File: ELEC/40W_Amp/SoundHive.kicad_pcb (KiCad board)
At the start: 2 copper layers, 5 parts, among them J1 CONN_01X08, J2 CONN_01X08, U1 TPA3106D1

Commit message: Parts and stuff
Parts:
- added C1: 1.0uF, Capacitors_SMD:C_0805, F.Cu at (97.8, 95.2)
- added C2: 1.0uF, Capacitors_SMD:C_0805, F.Cu at (97.8, 100.3)
- L1, L2: value XAL6060-333ME 33uH -> 33uH
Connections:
- U1 pad 19: Net-(U1-Pad19) -> Net-(L1-Pad1)
- U1 pad 20: Net-(U1-Pad20) -> Net-(L1-Pad1)
- U1 pad 21: Net-(U1-Pad21) -> Net-(L2-Pad1)
- U1 pad 22: Net-(U1-Pad22) -> Net-(L2-Pad1)
- U1 pad 3: Net-(U1-Pad3) -> GND
- U1 pad 4: Net-(U1-Pad4) -> GND
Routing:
- net Net-(C1-Pad1): track 0.00 -> 5.85 mm
- net Net-(C2-Pad1): track 0.00 -> 5.74 mm
- added copper zone on F.Cu, net Net-(L2-Pad1)

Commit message: Layout changes, Tall headers added
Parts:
- J1, J2: footprint Pin_Headers:Pin_Header_Straight_1x08_Pitch2.54mm -> Pin_Headers:Pin_Header_Straight_1x08_Tall_Pitch2.54mm

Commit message: Major work.
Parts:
- added C10: 0.22uF, Capacitors_SMD:C_0805, F.Cu at (131.6, 84.3)
- added C11: 0.22uF, Capacitors_SMD:C_0805, F.Cu at (123.4, 111.0)
- added C12: 1nF COG, Capacitors_SMD:C_0805, F.Cu at (102.9, 76.2)
- added C13: 1nF COG, Capacitors_SMD:C_0805, F.Cu at (95.5, 89.2)
- added C14: 1.0uF, Capacitors_SMD:C_0805, F.Cu at (101.6, 72.6)
- added C15: 1.0uF, Capacitors_SMD:C_0805, F.Cu at (116.3, 81.0)
- added C3: 220uF, Capacitors_SMD:CP_Elec_8x10.5, F.Cu at (114.3, 87.9)
- added C4: 1.0uF, Capacitors_SMD:C_0805, F.Cu at (112.3, 106.7)
- added C5: 220uF, Capacitors_SMD:CP_Elec_8x10.5, F.Cu at (114.6, 112.5)
- added C6: 1.0uF, Capacitors_SMD:C_0805, F.Cu at (112.3, 94.2)
- added C7: 1.0uF, Capacitors_SMD:C_0805, F.Cu at (103.9, 108.5)
- added C8: 1.0uF, Capacitors_SMD:C_0805, F.Cu at (105.9, 108.5)
- added C9: 1.0uF, Capacitors_SMD:C_0805, F.Cu at (108.0, 108.5)
- added R1: 100K, Resistors_SMD:R_0805, F.Cu at (98.0, 106.7)
- added R2: 100K, Resistors_SMD:R_0805, F.Cu at (98.0, 108.7)
- added R3: 100K 1%, Resistors_SMD:R_0805, F.Cu at (101.9, 108.5)
- added R4: R, Resistors_SMD:R_0805, F.Cu at (99.8, 84.6)
- added R5: R, Resistors_SMD:R_0805, F.Cu at (91.4, 85.1)
- moved J2 37.0 mm to (123.4, 76.7), turned to 270 degrees
- moved J1 33.7 mm to (101.9, 121.2), turned to 90 degrees
- moved L2 4.57 mm to (120.7, 96.0)
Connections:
- U1 pad 12: Net-(U1-Pad12) -> GND
- U1 pad 14: Net-(U1-Pad14) -> +24V
- U1 pad 15: Net-(U1-Pad15) -> +24V
- U1 pad 16: Net-(U1-Pad16) -> GND
- U1 pad 17: Net-(U1-Pad17) -> GND
- U1 pad 24: Net-(U1-Pad24) -> GND
- U1 pad 25: Net-(U1-Pad25) -> GND
- U1 pad 26: Net-(U1-Pad26) -> +24V
- U1 pad 27: Net-(U1-Pad27) -> +24V
- U1 pad 28: Net-(U1-Pad28) -> +24V
- U1 pad 5: Net-(U1-Pad5) -> /GAIN0
- U1 pad 6: Net-(U1-Pad6) -> /GAIN1

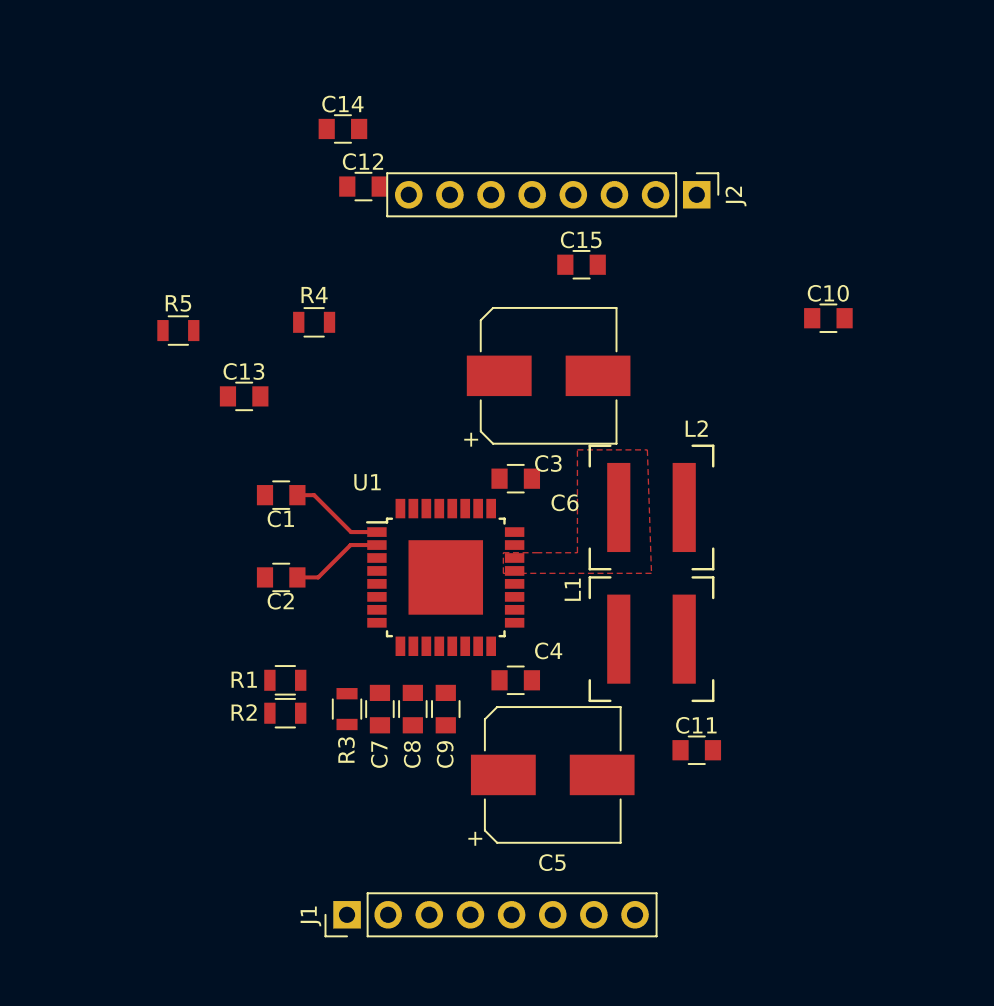
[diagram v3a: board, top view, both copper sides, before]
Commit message: Changed paths (Used  ${KIPRJMOD})
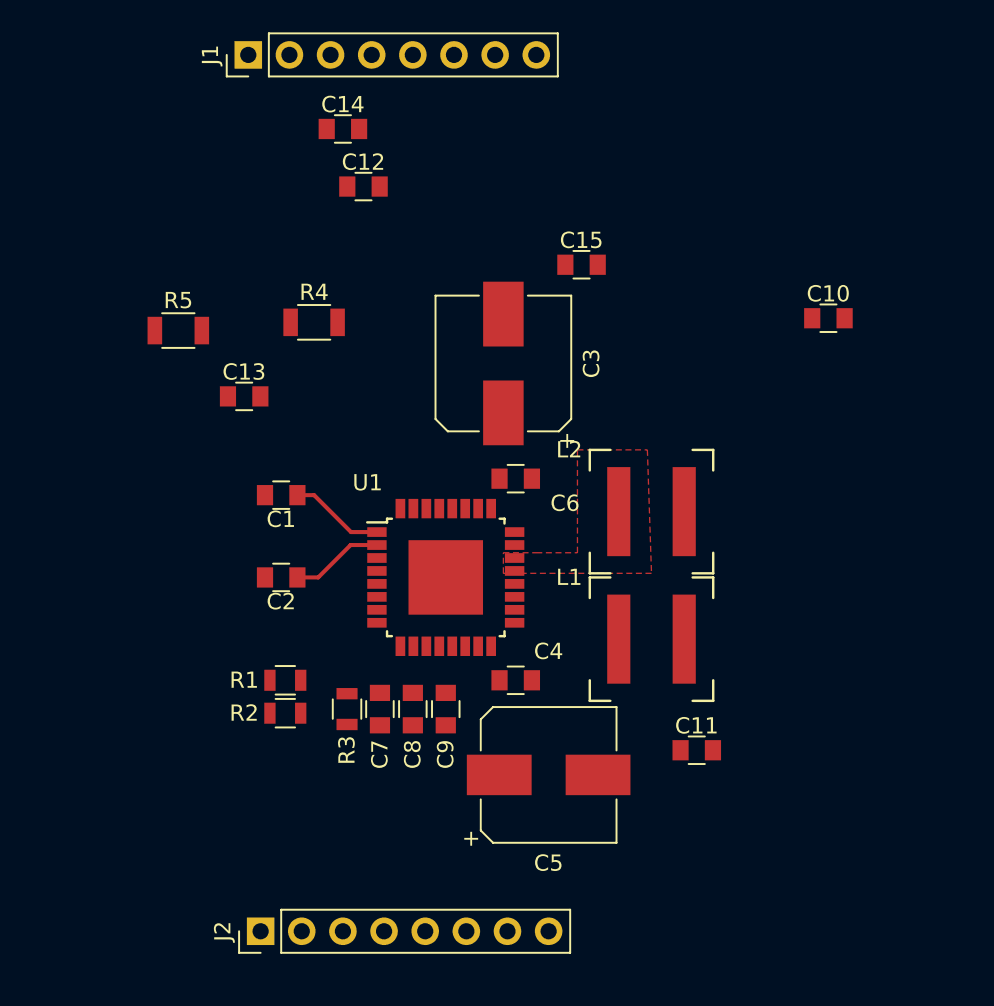
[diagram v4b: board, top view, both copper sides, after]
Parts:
- R4, R5: value R -> 20R 1/4 W, 5%; footprint Resistors_SMD:R_0805 -> Resistors_SMD:R_1206
- moved J1 53.4 mm to (95.8, 68.1)
- moved J2 52.8 mm to (96.5, 122.2), turned to 90 degrees
- moved C3 2.90 mm to (111.5, 87.1), turned to 90 degrees
- moved C5 0.25 mm to (114.3, 112.5)
- moved L2 0.25 mm to (120.7, 96.3)

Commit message: Added connector, redecorated.
Consider changing 2.54mm pich headers to somethin smaller
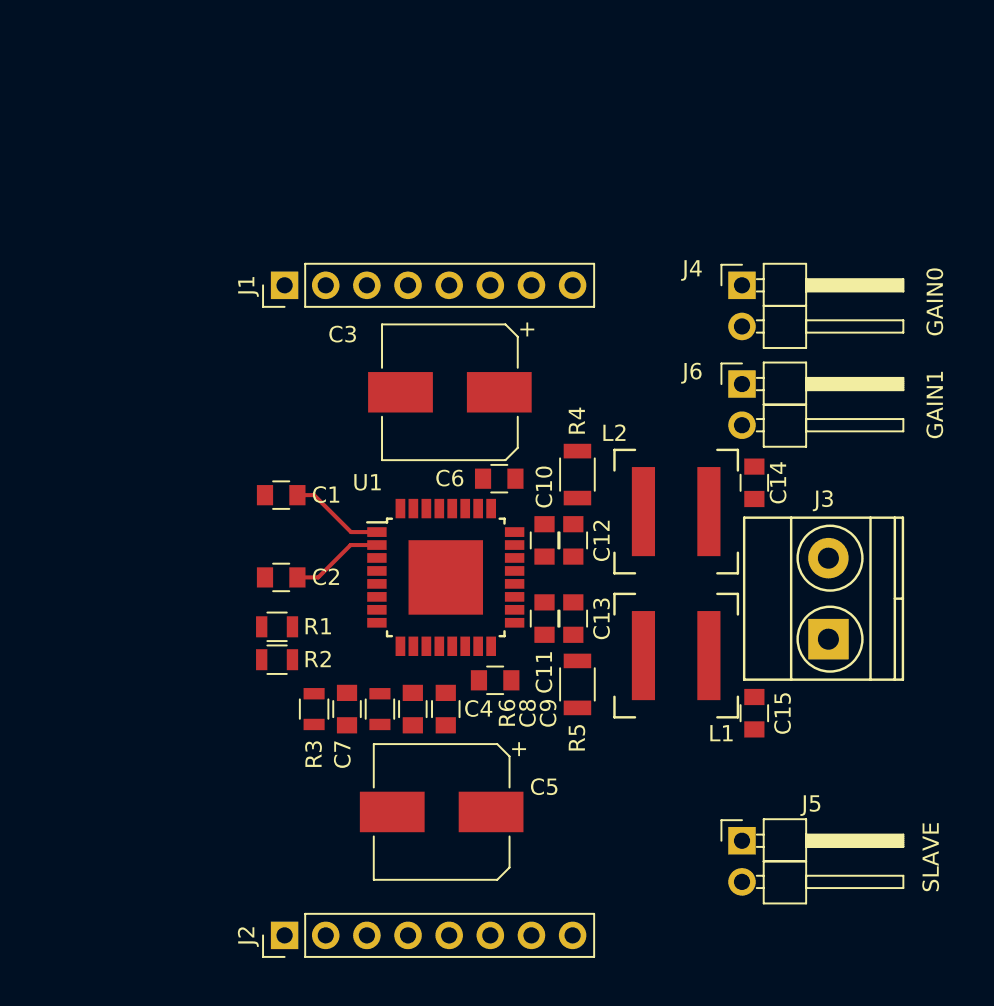
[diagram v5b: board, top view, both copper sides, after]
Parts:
- added J3: Screw_Terminal_1x02, Connectors_Terminal_Blocks.pretty:TerminalBlock_Pheonix_MKDS1.5-2pol, F.Cu at (131.6, 104.1)
- added J4: CONN_01X02_MALE, Pin_Headers:Pin_Header_Angled_1x02_Pitch2.54mm, F.Cu at (126.2, 82.3)
- added J5: CONN_01X02_MALE, Pin_Headers:Pin_Header_Angled_1x02_Pitch2.54mm, F.Cu at (126.2, 116.6)
- added J6: CONN_01X02_MALE, Pin_Headers:Pin_Header_Angled_1x02_Pitch2.54mm, F.Cu at (126.2, 88.4)
- added R6: 100K, Resistors_SMD:R_0805, F.Cu at (103.9, 108.5)
- moved C14 33.5 mm to (127.0, 94.5), turned to 270 degrees
- moved R5 32.9 mm to (116.1, 106.9), turned to 270 degrees
- moved C15 29.7 mm to (127.0, 108.7), turned to 270 degrees
- moved C12 25.4 mm to (115.8, 98.0), turned to 90 degrees
- moved C13 24.5 mm to (115.8, 102.9), turned to 90 degrees
- moved C10 22.3 mm to (114.0, 98.0), turned to 90 degrees
- moved R4 18.8 mm to (116.1, 94.0), turned to 270 degrees
- moved J1 14.4 mm to (98.0, 82.3)
- moved C11 12.4 mm to (114.0, 102.9), turned to 90 degrees
- moved C5 6.99 mm to (107.7, 114.8), turned to 180 degrees
- moved C3 3.75 mm to (108.2, 88.9), turned to 180 degrees
- moved R1 3.34 mm to (97.5, 103.4)
- moved R2 3.34 mm to (97.5, 105.4)
- moved C7 2.03 mm to (101.9, 108.5)
- moved R3 2.03 mm to (99.8, 108.5)
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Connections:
- J2 pad 7: Net-(J2-Pad7) -> GND
- J2 pad 8: Net-(J2-Pad8) -> /SYNC
- U1 pad 7: Net-(U1-Pad7) -> /SLV
- U1 pad 8: Net-(U1-Pad8) -> /SYNC
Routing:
- removed copper zone on F.Cu, net Net-(C10-Pad1)
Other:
- board text added: "GAIN0"
- board text added: "GAIN1"
- board text added: "SLAVE"

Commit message: -Moved all 3D models into project -This should be how we move forward. System paths are too flakey
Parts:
- added C16: 10uF, Capacitors_SMD:C_0805, F.Cu at (101.1, 93.0)
- added C17: 1.0uF, Capacitors_SMD:C_0805, F.Cu at (101.1, 91.2)
- added J7: CONN_01X03_MALE, Pin_Headers:Pin_Header_Angled_1x03_Pitch2.54mm, F.Cu at (120.4, 114.3)
- moved J5 27.0 mm to (132.8, 90.4), turned to 90 degrees
- moved J4 10.2 mm to (120.1, 90.4), turned to 90 degrees
- moved J6 2.05 mm to (126.5, 90.4), turned to 90 degrees
- moved J1 2.03 mm to (98.0, 80.3)
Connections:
- C2 pad 2: Net-(C2-Pad2) -> GND
- J1 pad 1: Net-(J1-Pad1) -> +24V
- J1 pad 2: Net-(J1-Pad2) -> +24V
- J1 pad 3: Net-(J1-Pad3) -> +24V
- J1 pad 4: Net-(J1-Pad4) -> +24V
- J1 pad 5: Net-(J1-Pad5) -> GND
- J1 pad 6: Net-(J1-Pad6) -> GND
- J1 pad 7: Net-(J1-Pad7) -> GND
- J1 pad 8: Net-(J1-Pad8) -> GND
- J2 pad 5: Net-(J2-Pad5) -> /AUX_L
- J2 pad 6: Net-(J2-Pad6) -> /AUX_R
- U1 pad 32: Net-(U1-Pad32) -> +24V
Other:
- board text added: "Left"
- board text added: "Out"
- board text added: "Right"

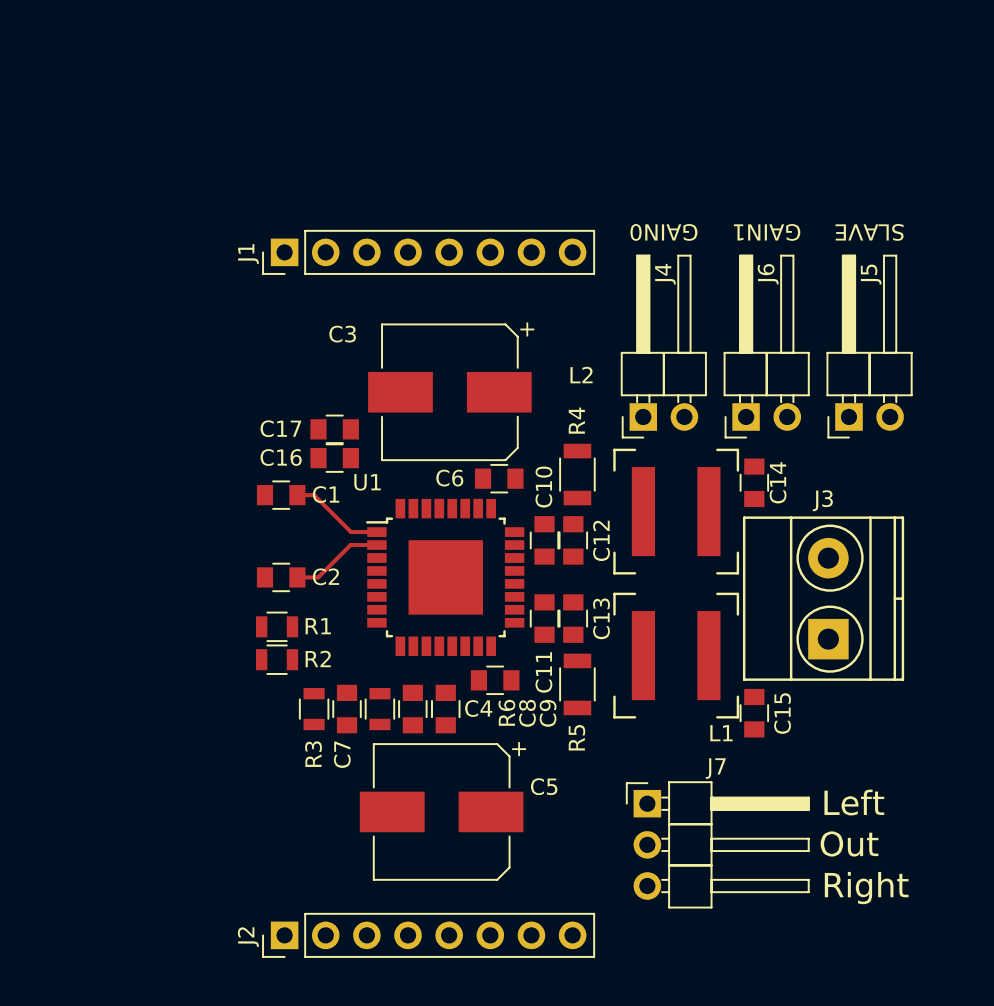
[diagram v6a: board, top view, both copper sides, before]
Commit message: V1.01, board ordered. June 14th, 2017, OSH Park.
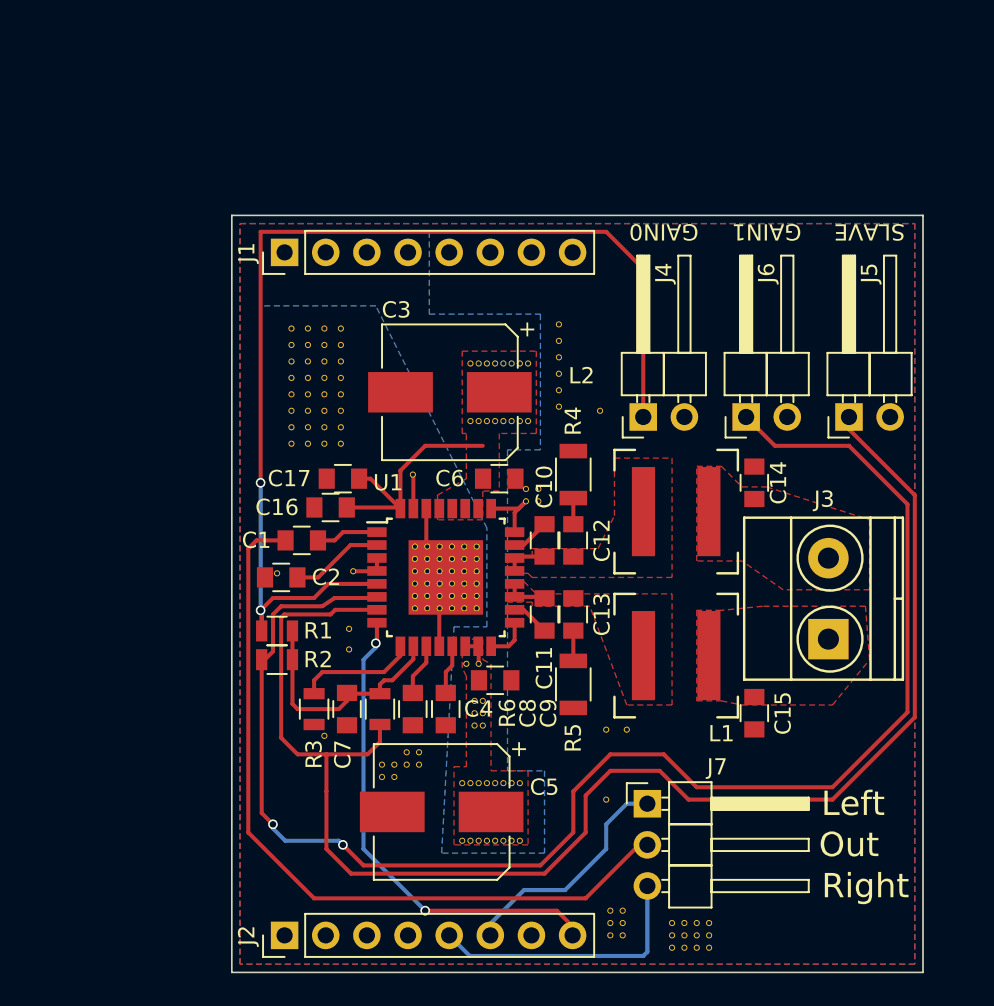
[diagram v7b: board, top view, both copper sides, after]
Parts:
- added J8: CONN_01X01, Via:10mil_Via, F.Cu at (105.9, 94.0)
- added REF**: Vias, Via:10mil_Via, F.Cu at (118.9, 120.9)
- added REF**: Vias, Via:10mil_Via, F.Cu at (124.2, 121.7)
- added REF**: Vias, Via:10mil_Via, F.Cu at (112.0, 87.1)
- added REF**: Vias, Via:10mil_Via, F.Cu at (111.5, 87.1)
- added REF**: Vias, Via:10mil_Via, F.Cu at (109.0, 116.6)
- added REF**: Vias, Via:10mil_Via, F.Cu at (109.5, 116.6)
- added REF**: Vias, Via:10mil_Via, F.Cu at (110.5, 116.6)
- added REF**: Vias, Via:10mil_Via, F.Cu at (110.0, 116.6)
- added REF**: Vias, Via:10mil_Via, F.Cu at (112.0, 116.6)
- added REF**: Vias, Via:10mil_Via, F.Cu at (112.5, 116.6)
- added REF**: Vias, Via:10mil_Via, F.Cu at (111.5, 116.6)
- added REF**: Vias, Via:10mil_Via, F.Cu at (111.0, 116.6)
- added REF**: Vias, Via:10mil_Via, F.Cu at (124.2, 122.4)
- added REF**: Vias, Via:10mil_Via, F.Cu at (111.0, 113.0)
- added REF**: Vias, Via:10mil_Via, F.Cu at (111.5, 113.0)
- added REF**: Vias, Via:10mil_Via, F.Cu at (112.5, 113.0)
- added REF**: Vias, Via:10mil_Via, F.Cu at (112.0, 113.0)
- added REF**: Vias, Via:10mil_Via, F.Cu at (110.0, 113.0)
- added REF**: Vias, Via:10mil_Via, F.Cu at (110.5, 113.0)
- added REF**: Vias, Via:10mil_Via, F.Cu at (109.5, 113.0)
- added REF**: Vias, Via:10mil_Via, F.Cu at (109.0, 113.0)
- added REF**: Vias, Via:10mil_Via, F.Cu at (106.8, 98.4)
- added REF**: Vias, Via:10mil_Via, F.Cu at (106.0, 98.4)
- added REF**: Vias, Via:10mil_Via, F.Cu at (122.7, 122.4)
- added REF**: Vias, Via:10mil_Via, F.Cu at (107.6, 98.4)
- added REF**: Vias, Via:10mil_Via, F.Cu at (108.3, 98.4)
- added REF**: Vias, Via:10mil_Via, F.Cu at (109.9, 98.4)
- added REF**: Vias, Via:10mil_Via, F.Cu at (109.1, 98.4)
- added REF**: Vias, Via:10mil_Via, F.Cu at (109.1, 99.2)
- added REF**: Vias, Via:10mil_Via, F.Cu at (109.9, 99.2)
- added REF**: Vias, Via:10mil_Via, F.Cu at (108.3, 99.2)
- added REF**: Vias, Via:10mil_Via, F.Cu at (107.6, 99.2)
- added REF**: Vias, Via:10mil_Via, F.Cu at (106.0, 99.2)
- added REF**: Vias, Via:10mil_Via, F.Cu at (106.8, 99.2)
- added REF**: Vias, Via:10mil_Via, F.Cu at (122.7, 121.7)
- added REF**: Vias, Via:10mil_Via, F.Cu at (106.8, 99.9)
- added REF**: Vias, Via:10mil_Via, F.Cu at (106.0, 99.9)
- added REF**: Vias, Via:10mil_Via, F.Cu at (107.6, 99.9)
- added REF**: Vias, Via:10mil_Via, F.Cu at (108.3, 99.9)
- added REF**: Vias, Via:10mil_Via, F.Cu at (109.9, 99.9)
- added REF**: Vias, Via:10mil_Via, F.Cu at (109.1, 99.9)
- added REF**: Vias, Via:10mil_Via, F.Cu at (109.1, 100.7)
- added REF**: Vias, Via:10mil_Via, F.Cu at (109.9, 100.7)
- added REF**: Vias, Via:10mil_Via, F.Cu at (108.3, 100.7)
- added REF**: Vias, Via:10mil_Via, F.Cu at (107.6, 100.7)
- added REF**: Vias, Via:10mil_Via, F.Cu at (121.9, 121.7)
- added REF**: Vias, Via:10mil_Via, F.Cu at (106.0, 100.7)
- added REF**: Vias, Via:10mil_Via, F.Cu at (106.8, 100.7)
- added REF**: Vias, Via:10mil_Via, F.Cu at (106.8, 102.2)
- added REF**: Vias, Via:10mil_Via, F.Cu at (106.0, 102.2)
- added REF**: Vias, Via:10mil_Via, F.Cu at (107.6, 102.2)
- added REF**: Vias, Via:10mil_Via, F.Cu at (108.3, 102.2)
- added REF**: Vias, Via:10mil_Via, F.Cu at (109.9, 102.2)
- added REF**: Vias, Via:10mil_Via, F.Cu at (109.1, 102.2)
- added REF**: Vias, Via:10mil_Via, F.Cu at (109.1, 101.5)
- added REF**: Vias, Via:10mil_Via, F.Cu at (109.9, 101.5)
- added REF**: Vias, Via:10mil_Via, F.Cu at (104.0, 111.9)
- added REF**: Vias, Via:10mil_Via, F.Cu at (108.3, 101.5)
- added REF**: Vias, Via:10mil_Via, F.Cu at (107.6, 101.5)
- added REF**: Vias, Via:10mil_Via, F.Cu at (106.0, 101.5)
- added REF**: Vias, Via:10mil_Via, F.Cu at (106.8, 101.5)
- added REF**: Vias, Via:10mil_Via, F.Cu at (104.8, 111.9)
- added REF**: Vias, Via:10mil_Via, F.Cu at (104.8, 112.6)
- added REF**: Vias, Via:10mil_Via, F.Cu at (104.0, 112.6)
- added REF**: Vias, Via:10mil_Via, F.Cu at (105.5, 111.9)
- added REF**: Vias, Via:10mil_Via, F.Cu at (118.1, 122.4)
- added REF**: Vias, Via:10mil_Via, F.Cu at (106.3, 111.9)
- added REF**: Vias, Via:10mil_Via, F.Cu at (113.7, 95.6)
- added REF**: Vias, Via:10mil_Via, F.Cu at (112.9, 95.6)
- added REF**: Vias, Via:10mil_Via, F.Cu at (112.9, 94.9)
- added REF**: Vias, Via:10mil_Via, F.Cu at (113.7, 94.9)
- added REF**: Vias, Via:10mil_Via, F.Cu at (106.3, 111.1)
- added REF**: Vias, Via:10mil_Via, F.Cu at (105.5, 111.1)
- added REF**: Vias, Via:10mil_Via, F.Cu at (100.5, 110.1)
- added REF**: Vias, Via:10mil_Via, F.Cu at (114.9, 85.7)
- added REF**: Vias, Via:10mil_Via, F.Cu at (114.9, 89.8)
- added REF**: Vias, Via:10mil_Via, F.Cu at (118.1, 121.7)
- added REF**: Vias, Via:10mil_Via, F.Cu at (114.9, 88.8)
- added REF**: Vias, Via:10mil_Via, F.Cu at (114.9, 86.7)
- added REF**: Vias, Via:10mil_Via, F.Cu at (114.9, 87.8)
- added REF**: Vias, Via:10mil_Via, F.Cu at (98.4, 90.0)
- added REF**: Vias, Via:10mil_Via, F.Cu at (98.4, 89.0)
- added REF**: Vias, Via:10mil_Via, F.Cu at (98.4, 91.1)
- added REF**: Vias, Via:10mil_Via, F.Cu at (98.4, 92.1)
- added REF**: Vias, Via:10mil_Via, F.Cu at (99.4, 92.1)
- added REF**: Vias, Via:10mil_Via, F.Cu at (99.4, 91.1)
- added REF**: Vias, Via:10mil_Via, F.Cu at (99.4, 89.0)
- added REF**: Vias, Via:10mil_Via, F.Cu at (121.9, 123.2)
- added REF**: Vias, Via:10mil_Via, F.Cu at (99.4, 90.0)
- added REF**: Vias, Via:10mil_Via, F.Cu at (101.5, 90.0)
- added REF**: Vias, Via:10mil_Via, F.Cu at (101.5, 89.0)
- added REF**: Vias, Via:10mil_Via, F.Cu at (101.5, 91.1)
- added REF**: Vias, Via:10mil_Via, F.Cu at (101.5, 92.1)
- added REF**: Vias, Via:10mil_Via, F.Cu at (100.5, 92.1)
- added REF**: Vias, Via:10mil_Via, F.Cu at (100.5, 91.1)
- added REF**: Vias, Via:10mil_Via, F.Cu at (100.5, 89.0)
- added REF**: Vias, Via:10mil_Via, F.Cu at (100.5, 90.0)
- added REF**: Vias, Via:10mil_Via, F.Cu at (100.5, 86.0)
- added REF**: Vias, Via:10mil_Via, F.Cu at (122.7, 123.2)
- added REF**: Vias, Via:10mil_Via, F.Cu at (100.5, 85.0)
- added REF**: Vias, Via:10mil_Via, F.Cu at (100.5, 87.0)
- added REF**: Vias, Via:10mil_Via, F.Cu at (100.5, 88.0)
- added REF**: Vias, Via:10mil_Via, F.Cu at (101.5, 88.0)
- added REF**: Vias, Via:10mil_Via, F.Cu at (101.5, 87.0)
- added REF**: Vias, Via:10mil_Via, F.Cu at (101.5, 85.0)
- added REF**: Vias, Via:10mil_Via, F.Cu at (101.5, 86.0)
- added REF**: Vias, Via:10mil_Via, F.Cu at (99.4, 86.0)
- added REF**: Vias, Via:10mil_Via, F.Cu at (99.4, 85.0)
- added REF**: Vias, Via:10mil_Via, F.Cu at (99.4, 87.0)
- added REF**: Vias, Via:10mil_Via, F.Cu at (124.2, 123.2)
- added REF**: Vias, Via:10mil_Via, F.Cu at (99.4, 88.0)
- added REF**: Vias, Via:10mil_Via, F.Cu at (98.4, 88.0)
- added REF**: Vias, Via:10mil_Via, F.Cu at (98.4, 87.0)
- added REF**: Vias, Via:10mil_Via, F.Cu at (110.0, 105.7)
- added REF**: Vias, Via:10mil_Via, F.Cu at (110.2, 109.5)
- added REF**: Vias, Via:10mil_Via, F.Cu at (109.7, 109.5)
- added REF**: Vias, Via:10mil_Via, F.Cu at (109.7, 108.7)
- added REF**: Vias, Via:10mil_Via, F.Cu at (110.2, 108.7)
- added REF**: Vias, Via:10mil_Via, F.Cu at (110.2, 108.0)
- added REF**: Vias, Via:10mil_Via, F.Cu at (109.7, 108.0)
- added REF**: Vias, Via:10mil_Via, F.Cu at (123.4, 123.2)
- added REF**: Vias, Via:10mil_Via, F.Cu at (109.2, 105.7)
- added REF**: Vias, Via:10mil_Via, F.Cu at (121.9, 122.4)
- added REF**: Vias, Via:10mil_Via, F.Cu at (118.1, 120.9)
- added REF**: Vias, Via:10mil_Via, F.Cu at (117.9, 114.0)
- added REF**: Vias, Via:10mil_Via, F.Cu at (117.9, 109.7)
- added REF**: Vias, Via:10mil_Via, F.Cu at (119.1, 109.7)
- added REF**: Vias, Via:10mil_Via, F.Cu at (118.9, 121.7)
- added REF**: Vias, Via:10mil_Via, F.Cu at (118.9, 122.4)
- added REF**: Vias, Via:10mil_Via, F.Cu at (97.5, 100.1)
- added REF**: Vias, Via:10mil_Via, F.Cu at (102.0, 104.8)
- added REF**: Vias, Via:10mil_Via, F.Cu at (123.4, 122.4)
- added REF**: Vias, Via:10mil_Via, F.Cu at (102.0, 103.5)
- added REF**: Vias, Via:10mil_Via, F.Cu at (102.2, 99.9)
- added REF**: Vias, Via:10mil_Via, F.Cu at (117.5, 90.0)
- added REF**: Vias, Via:10mil_Via, F.Cu at (114.9, 84.7)
- added REF**: Vias, Via:10mil_Via, F.Cu at (98.4, 85.0)
- added REF**: Vias, Via:10mil_Via, F.Cu at (98.4, 86.0)
- added REF**: Vias, Via:10mil_Via, F.Cu at (111.5, 90.7)
- added REF**: Vias, Via:10mil_Via, F.Cu at (112.0, 90.7)
- added REF**: Vias, Via:10mil_Via, F.Cu at (113.0, 90.7)
- added REF**: Vias, Via:10mil_Via, F.Cu at (112.5, 90.7)
- added REF**: Vias, Via:10mil_Via, F.Cu at (123.4, 121.7)
- added REF**: Vias, Via:10mil_Via, F.Cu at (110.5, 90.7)
- added REF**: Vias, Via:10mil_Via, F.Cu at (111.0, 90.7)
- added REF**: Vias, Via:10mil_Via, F.Cu at (110.0, 90.7)
- added REF**: Vias, Via:10mil_Via, F.Cu at (109.5, 90.7)
- added REF**: Vias, Via:10mil_Via, F.Cu at (109.5, 87.1)
- added REF**: Vias, Via:10mil_Via, F.Cu at (110.0, 87.1)
- added REF**: Vias, Via:10mil_Via, F.Cu at (111.0, 87.1)
- added REF**: Vias, Via:10mil_Via, F.Cu at (110.5, 87.1)
- added REF**: Vias, Via:10mil_Via, F.Cu at (112.5, 87.1)
- added REF**: Vias, Via:10mil_Via, F.Cu at (113.0, 87.1)
- moved C17 3.09 mm to (101.6, 94.2)
- moved C1 3.07 mm to (99.1, 98.0)
- moved C16 3.06 mm to (100.8, 96.0)
- moved C11 0.25 mm to (114.0, 102.6)
- moved C13 0.25 mm to (115.8, 102.6)
- moved R1 0.25 mm to (97.5, 103.6)
- moved R4 0.25 mm to (115.8, 94.0)
- moved R5 0.25 mm to (115.8, 106.9)
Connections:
- C1 pad 2: Net-(C1-Pad2) -> /LR_MuxOut
- U1 pad 29: Net-(U1-Pad29) -> +24V
- U1 pad 30: Net-(U1-Pad30) -> GND
- U1 pad 33: Net-(U1-Pad33) -> GND
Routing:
- net /GAIN1: track 0.00 -> 92.9 mm, vias 0 -> 2
- net /SLV: track 0.00 -> 91.3 mm
- net /GAIN0: track 0.00 -> 67.4 mm, vias 0 -> 2
- net /LR_MuxOut: track 0.00 -> 47.7 mm
- net /SYNC: track 0.00 -> 29.8 mm, vias 0 -> 2
- net /AUX_L: track 0.00 -> 16.9 mm
- net +24V: track 0.00 -> 16.6 mm
- net Net-(C7-Pad2): track 0.00 -> 15.1 mm
- net /AUX_R: track 0.00 -> 14.4 mm
- net GND: track 0.00 -> 14.2 mm
- net Net-(R3-Pad1): track 0.00 -> 7.37 mm
- net Net-(C8-Pad2): track 0.00 -> 3.22 mm
- net Net-(C9-Pad2): track 0.00 -> 3.04 mm
- net Net-(C10-Pad1): track 0.00 -> 2.68 mm
- net Net-(C11-Pad2): track 0.00 -> 2.68 mm
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- added copper zone on B.Cu, net +24V
- added copper zone on F.Cu, net +24V
- added copper zone on B.Cu, net GND
- added copper zone on F.Cu, net GND
- added copper zone on F.Cu, net Net-(C10-Pad1)
- added copper zone on F.Cu, net Net-(C11-Pad2)
- added copper zone on F.Cu, net Net-(C14-Pad2)
- added copper zone on F.Cu, net Net-(C15-Pad1)
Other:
- board outline added: 42.7 x 46.7 mm
